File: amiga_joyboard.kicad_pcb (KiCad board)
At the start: 2 copper layers, 192.5 x 63.5 mm, 27 parts, among them J1 JOYPORT_OUT, J2 CONN_D, J3 CONN_F, SW1 FIRE_BTN, SW2 B_BTN, SW3 A_BTN, SW4 RIGHT_BTN, SW5 LEFT_BTN, SW6 DOWN_BTN, SW7 UP_BTN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

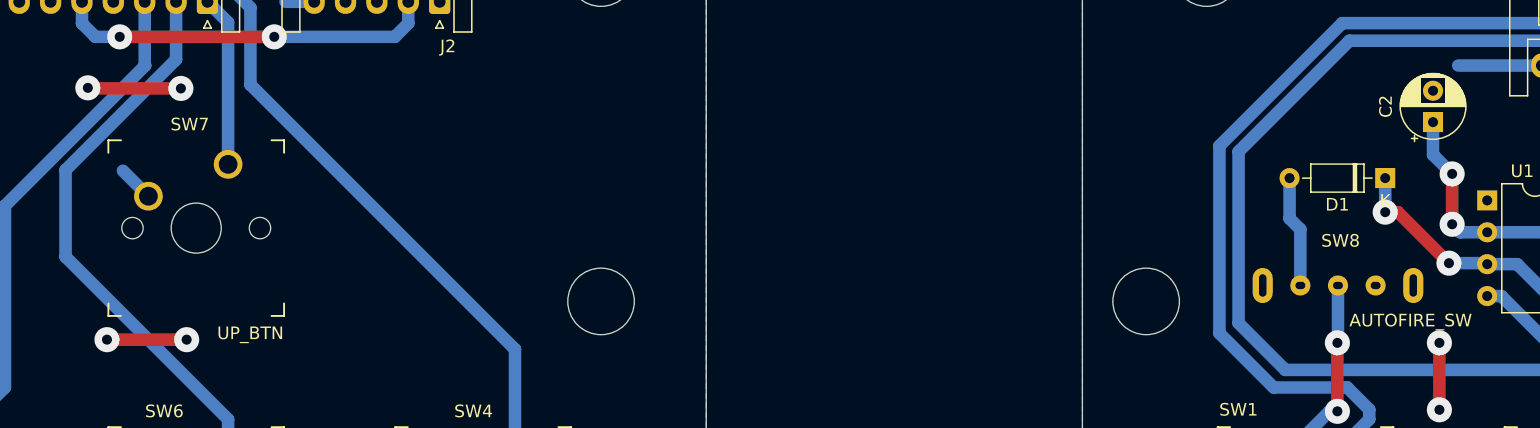
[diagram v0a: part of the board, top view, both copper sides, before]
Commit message: unnecessary jumpers removed, cosmetics
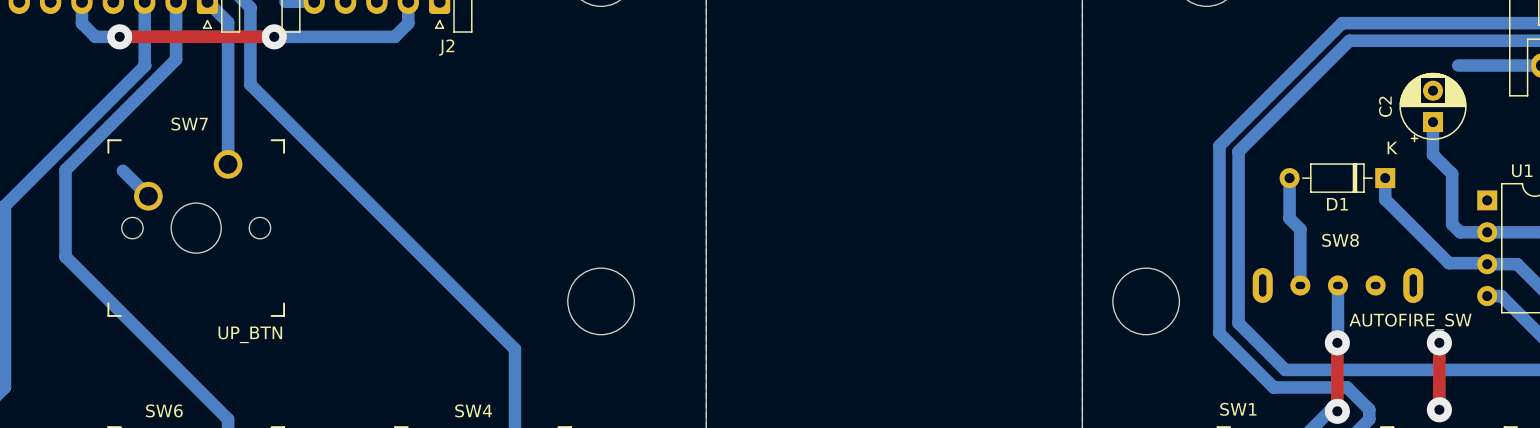
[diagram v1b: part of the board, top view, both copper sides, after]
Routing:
- net GND_D: track 60.3 -> 46.2 mm, vias 4 -> 0
- net /AUTOFIRE: track 34.6 -> 34.0 mm, vias 2 -> 0
- net Net-(U1-THR): vias 2 -> 0
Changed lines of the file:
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@@
 			)
 		)
-		(attr exclude_from_pos_files exclude_from_bom)
+		(attr board_only exclude_from_pos_files exclude_from_bom)
 		(fp_circle
 			(center 0 0)
@@
 			)
 		)
-		(attr exclude_from_pos_files exclude_from_bom)
+		(attr board_only exclude_from_pos_files exclude_from_bom)
 		(fp_circle
 			(center 0 0)
@@
 			)
 		)
-		(attr exclude_from_pos_files exclude_from_bom)
+		(attr board_only exclude_from_pos_files exclude_from_bom)
 		(fp_circle
 			(center 0 0)
@@
 			)
 		)
-		(attr exclude_from_pos_files exclude_from_bom)
+		(attr board_only exclude_from_pos_files exclude_from_bom)
 		(fp_circle
 			(center 0 0)
@@
 			)
 		)
-		(attr exclude_from_pos_files exclude_from_bom)
+		(attr board_only exclude_from_pos_files exclude_from_bom)
 		(fp_circle
 			(center 0 0)
@@
 		)
 		(fp_text user "K"
-			(at 0 -1.8 0)
+			(at -0.508 2.366 0)
 			(layer "F.SilkS")
 			(effects
@@
 			)
 		)
-		(fp_text user "K"
-			(at 0 -1.8 0)
-			(layer "F.Fab")
-			(effects
-				(font
-					(size 1 1)
-					(thickness 0.15)
-				)
-			)
-		)
 		(pad "1" thru_hole rect
 			(at 0 0 180)
@@
 			)
 		)
-		(attr exclude_from_pos_files exclude_from_bom)
+		(attr board_only exclude_from_pos_files exclude_from_bom)
 		(fp_circle
 			(center 0 0)
@@
 			)
 		)
-		(attr exclude_from_pos_files exclude_from_bom)
+		(attr board_only exclude_from_pos_files exclude_from_bom)
 		(fp_circle
 			(center 0 0)
@@
 	)
 	(segment
-		(start 189.738 91.44)
-		(end 189.738 95.452)
-		(width 1)
-		(layer "F.Cu")
-		(net 3)
-	)
-	(via
-		(at 189.738 91.44)
-		(size 2)
-		(drill 0.8)
-		(layers "F.Cu" "B.Cu")
-		(net 3)
-	)
-	(via
-		(at 189.738 95.452)
-		(size 2)
-		(drill 0.8)
-		(layers "F.Cu" "B.Cu")
-		(net 3)
-	)
-	(segment
 		(start 196.965899 96.092)
 		(end 199.505899 98.632)
@@
 	)
 	(segment
+		(start 189.738 91.44)
+		(end 189.738 95.452)
+		(width 1)
+		(layer "B.Cu")
+		(net 3)
+	)
+	(segment
 		(start 219.964 97.282)
 		(end 221.648 97.282)
@@
 	)
 	(segment
-		(start 184.404 94.488)
-		(end 185.42 94.488)
-		(width 1)
-		(layer "F.Cu")
-		(net 5)
-	)
-	(segment
-		(start 185.42 94.488)
-		(end 189.484 98.552)
-		(width 1)
-		(layer "F.Cu")
-		(net 5)
-	)
-	(via
-		(at 189.484 98.552)
-		(size 2)
-		(drill 0.8)
-		(layers "F.Cu" "B.Cu")
-		(net 5)
-	)
-	(via
-		(at 184.404 94.488)
-		(size 2)
-		(drill 0.8)
-		(layers "F.Cu" "B.Cu")
-		(net 5)
-	)
-	(segment
 		(start 192.532 98.632)
 		(end 194.924994 98.632)
@@
 	)
 	(segment
-		(start 184.404 91.774)
-		(end 184.404 94.488)
+		(start 192.452 98.552)
+		(end 192.532 98.632)
 		(width 1)
 		(layer "B.Cu")
@@
 	)
 	(segment
-		(start 192.452 98.552)
-		(end 192.532 98.632)
+		(start 184.404 93.472)
+		(end 189.484 98.552)
+		(width 1)
+		(layer "B.Cu")
+		(net 5)
+	)
+	(segment
+		(start 184.404 91.774)
+		(end 184.404 93.472)
 		(width 1)
 		(layer "B.Cu")
@@
 	)
 	(segment
-		(start 88.439452 84.629452)
-		(end 81.073452 84.629452)
-		(width 1)
-		(layer "F.Cu")
-		(net 9)
-	)
-	(segment
-		(start 88.9 104.648)
-		(end 82.55 104.648)
-		(width 1)
-		(layer "F.Cu")
-		(net 9)
-	)
-	(segment
-		(start 81.073452 84.629452)
-		(end 81.026 84.582)
-		(width 1)
-		(layer "F.Cu")
-		(net 9)
-	)
-	(via
-		(at 82.55 104.648)
-		(size 2)
-		(drill 0.8)
-		(layers "F.Cu" "B.Cu")
-		(net 9)
-	)
-	(via
-		(at 88.9 104.648)
-		(size 2)
-		(drill 0.8)
-		(layers "F.Cu" "B.Cu")
-		(net 9)
-	)
-	(via
-		(at 88.439452 84.629452)
-		(size 2)
-		(drill 0.8)
-		(layers "F.Cu" "B.Cu")
-		(net 9)
-	)
-	(via
-		(at 81.026 84.582)
-		(size 2)
-		(drill 0.8)
-		(layers "F.Cu" "B.Cu")
-		(net 9)
-	)
-	(segment
 		(start 94.343497 71.229497)
 		(end 94.343497 73.261497)
@@
 		(width 1)
 		(layer "B.Cu")
-		(net 9)
-	)
-	(segment
-		(start 82.55 104.648)
-		(end 82.826675 104.924675)
-		(width 1)
-		(layer "B.Cu")

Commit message: silly text
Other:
- board text added: "JoyBoard DirBoard v 1.0"
- board text added: "JoyBoard FireBoard"
- board text added: "Kot_Behemot 2024"
- board text added: "v 1.0"
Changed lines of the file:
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@@
 		(tags "connector JST XH horizontal")
 		(property "Reference" "J3"
-			(at 5 -3.5 360)
+			(at 5 -3.5 0)
 			(layer "F.SilkS")
 			(effects
@@
 		)
 		(fp_text user "${REFERENCE}"
-			(at 5 3.45 360)
+			(at 5 3.45 0)
 			(layer "F.Fab")
 			(effects
@@
 		(tags "connector JST XH horizontal")
 		(property "Reference" "J2"
-			(at -0.668 -3.556 360)
+			(at -0.668 -3.556 0)
 			(layer "F.SilkS")
 			(effects
@@
 		)
 		(fp_text user "${REFERENCE}"
-			(at 5 3.45 360)
+			(at 5 3.45 0)
 			(layer "F.Fab")
 			(effects
@@
 		(layer "Edge.Cuts")
 	)
+	(gr_text "Kot_Behemot 2024"
+		(at 78.486 85.598 0)
+		(layer "B.Cu" knockout)
+		(effects
+			(font
+				(size 1.9 1.9)
+				(thickness 0.4)
+				(bold yes)
+			)
+			(justify left bottom mirror)
+		)
+	)
+	(gr_text "JoyBoard FireBoard"
+		(at 190.5 69.85 0)
+		(layer "B.Cu" knockout)
+		(effects
+			(font
+				(size 1.9 1.9)
+				(thickness 0.4)
+				(bold yes)
+			)
+			(justify left bottom mirror)
+		)
+	)
+	(gr_text "Kot_Behemot 2024"
+		(at 227.33 70.104 0)
+		(layer "B.Cu" knockout)
+		(effects
+			(font
+				(size 1.9 1.9)
+				(thickness 0.4)
+				(bold yes)
+			)
+			(justify left bottom mirror)
+		)
+	)
+	(gr_text "JoyBoard DirBoard\nv 1.0"
+		(at 128.524 88.646 0)
+		(layer "B.Cu" knockout)
+		(effects
+			(font
+				(size 1.9 1.9)
+				(thickness 0.4)
+				(bold yes)
+			)
+			(justify left bottom mirror)
+		)
+	)
+	(gr_text "v 1.0"
+		(at 190.5 73.152 0)
+		(layer "B.Cu" knockout)
+		(effects
+			(font
+				(size 1.9 1.9)
+				(thickness 0.4)
+				(bold yes)
+			)
+			(justify left bottom mirror)
+		)
+	)
 	(segment

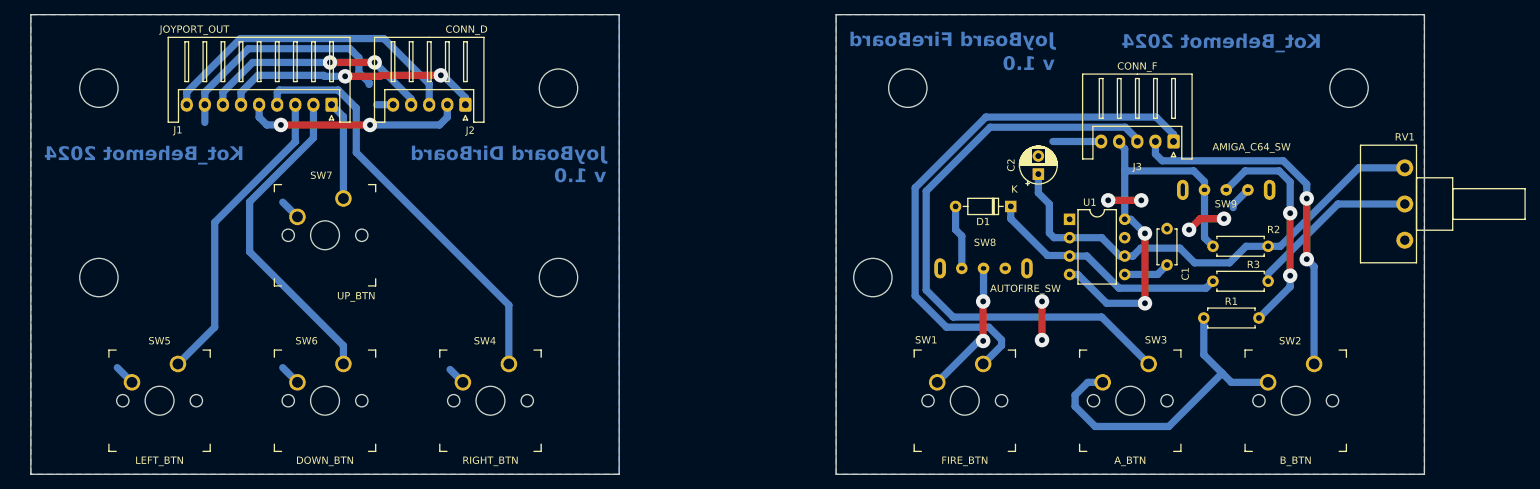
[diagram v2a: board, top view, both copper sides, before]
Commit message: footprints cleanup - kailh copied to local footprints dir
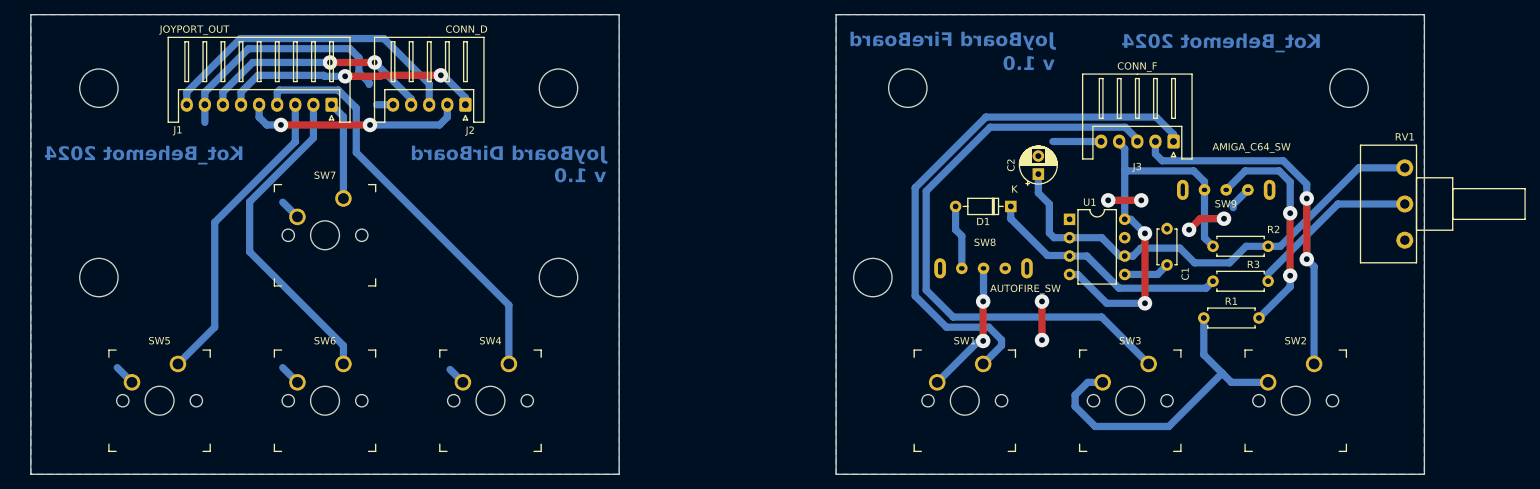
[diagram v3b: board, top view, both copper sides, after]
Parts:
- SW1, SW2, SW3, SW4, SW5, SW6, SW7: footprint Kailh:SW_MX -> Amiga Joyboard:SW_MX
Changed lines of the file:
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@@
 	(net 23 "/A_F")
 	(net 24 "/FIRE_F")
-	(footprint "Kailh:SW_MX"
+	(footprint "Amiga Joyboard:SW_MX"
 		(layer "F.Cu")
 		(at 66.802 118.618)
@@
 		(property "Value" "LEFT_BTN"
 			(at 0 8.255 0)
-			(layer "F.SilkS")
+			(layer "F.Fab")
 			(effects
 				(font
@@
 			)
 		)
-		(property "Footprint" "Kailh:SW_MX"
+		(property "Footprint" "Amiga Joyboard:SW_MX"
 			(at 0 0 0)
 			(layer "F.Fab")
@@
 		)
 	)
-	(footprint "Kailh:SW_MX"
+	(footprint "Amiga Joyboard:SW_MX"
 		(layer "F.Cu")
 		(at 178.054 118.618)
@@
 		(tags "MX,cherry,gateron,kailh")
 		(property "Reference" "SW1"
-			(at -5.334 -8.382 0)
+			(at 0 -8.255 0)
 			(layer "F.SilkS")
 			(effects
@@
 		(property "Value" "FIRE_BTN"
 			(at 0 8.255 0)
-			(layer "F.SilkS")
+			(layer "F.Fab")
 			(effects
 				(font
@@
 			)
 		)
-		(property "Footprint" "Kailh:SW_MX"
+		(property "Footprint" "Amiga Joyboard:SW_MX"
 			(at 0 0 0)
 			(layer "F.Fab")
@@
 		)
 	)
-	(footprint "Kailh:SW_MX"
+	(footprint "Amiga Joyboard:SW_MX"
 		(layer "F.Cu")
 		(at 89.662 95.758)
@@
 		(tags "MX,cherry,gateron,kailh")
 		(property "Reference" "SW7"
-			(at -0.508 -8.255 0)
+			(at 0 -8.255 0)
 			(layer "F.SilkS")
 			(effects
@@
 		)
 		(property "Value" "UP_BTN"
-			(at 4.318 8.382 0)
-			(layer "F.SilkS")
+			(at 0 8.255 0)
+			(layer "F.Fab")
 			(effects
 				(font
@@
 			)
 		)
-		(property "Footprint" "Kailh:SW_MX"
+		(property "Footprint" "Amiga Joyboard:SW_MX"
 			(at 0 0 0)
 			(layer "F.Fab")
@@
 		)
 	)
-	(footprint "Kailh:SW_MX"
+	(footprint "Amiga Joyboard:SW_MX"
 		(layer "F.Cu")
 		(at 223.774 118.618)
@@
 		(tags "MX,cherry,gateron,kailh")
 		(property "Reference" "SW2"
-			(at -0.762 -8.255 0)
+			(at 0 -8.255 0)
 			(layer "F.SilkS")
 			(effects
@@
 		(property "Value" "B_BTN"
 			(at 0 8.255 0)
-			(layer "F.SilkS")
+			(layer "F.Fab")
 			(effects
 				(font
@@
 			)
 		)
-		(property "Footprint" "Kailh:SW_MX"
+		(property "Footprint" "Amiga Joyboard:SW_MX"
 			(at 0 0 0)
 			(layer "F.Fab")
@@
 		)
 	)
-	(footprint "Kailh:SW_MX"
+	(footprint "Amiga Joyboard:SW_MX"
 		(layer "F.Cu")
 		(at 200.914 118.618)
@@
 		(tags "MX,cherry,gateron,kailh")
 		(property "Reference" "SW3"
-			(at 3.556 -8.382 0)
+			(at 0 -8.255 0)
 			(layer "F.SilkS")
 			(effects
@@
 		(property "Value" "A_BTN"
 			(at 0 8.255 0)
-			(layer "F.SilkS")
+			(layer "F.Fab")
 			(effects
 				(font
@@
 			)
 		)
-		(property "Footprint" "Kailh:SW_MX"
+		(property "Footprint" "Amiga Joyboard:SW_MX"
 			(at 0 0 0)
 			(layer "F.Fab")
@@
 		)
 	)
-	(footprint "Kailh:SW_MX"
+	(footprint "Amiga Joyboard:SW_MX"
 		(layer "F.Cu")
 		(at 89.662 118.618)
@@
 		(tags "MX,cherry,gateron,kailh")
 		(property "Reference" "SW6"
-			(at -2.54 -8.255 0)
+			(at 0 -8.255 0)
 			(layer "F.SilkS")
 			(effects
@@
 		(property "Value" "DOWN_BTN"
 			(at 0 8.255 0)
-			(layer "F.SilkS")
+			(layer "F.Fab")
 			(effects
 				(font
@@
 			)
 		)
-		(property "Footprint" "Kailh:SW_MX"
+		(property "Footprint" "Amiga Joyboard:SW_MX"
 			(at 0 0 0)
 			(layer "F.Fab")
@@
 		)
 	)
-	(footprint "Kailh:SW_MX"
+	(footprint "Amiga Joyboard:SW_MX"
 		(layer "F.Cu")
 		(at 112.522 118.618)
@@
 		(tags "MX,cherry,gateron,kailh")
 		(property "Reference" "SW4"
-			(at -0.762 -8.255 0)
+			(at 0 -8.255 0)
 			(layer "F.SilkS")
 			(effects
@@
 		(property "Value" "RIGHT_BTN"
 			(at 0 8.255 0)
-			(layer "F.SilkS")
+			(layer "F.Fab")
 			(effects
 				(font
@@
 			)
 		)
-		(property "Footprint" "Kailh:SW_MX"
+		(property "Footprint" "Amiga Joyboard:SW_MX"
 			(at 0 0 0)
 			(layer "F.Fab")
